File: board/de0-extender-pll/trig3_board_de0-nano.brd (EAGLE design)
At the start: 233.2 x 160 mm, 305 parts, among them IC1 ICL7660CPA, IC2 ICL7660CPA, IC3 ICL7660CPA, IC4 ICL7660CPA, J10 2p-2.54, J11 2p-2.54, J12 4p-2.54, J13 BU-SMB-V, J131 4p-2.54, J14 BU-SMB-V, J141 2p-2.54, J15 2p-2.54, J16 2p-2.54, J17 2p-2.54, J18 2p-2.54, J19 6HE-160-VG64AC, J20 4p-2.54, J21 4p-2.54, J22 2p-2.54, J23 2p-2.54, J24 2p-2.54, J25 2p-2.54, J26 4p-2.54, J27 4p-2.54, J28 2p-2.54, J29 2p-2.54, J3 4p-2.54, J30 2p-2.54, J31 2p-2.54, J311 4p-2.54, J32 2p-2.54, J33 2p-2.54, J34 2p-2.54, J35 2p-2.54, J36 2p-2.54, J37 2p-2.54, J38 2p-2.54, J39 2p-2.54, J4 2p-2.54, J40 2p-2.54, J41 2p-2.54, J42 2p-2.54, J43 2p-2.54, J48 2p-2.54, J49 2p-2.54, J5 2p-2.54, J50 2p-2.54, J51 2p-2.54, J52 2p-2.54, J53 2p-2.54, J54 2p-2.54, J55 2p-2.54, J6 2p-2.54, J7 4p-2.54, J8 2p-2.54, J9 2p-2.54, K15_R10P BU-SMB-V, K16_R10N BU-SMB-V, M16CLK_3N BU-SMB-V, P11 BU-SMB-V, P14_CLKOUT_4P BU-SMB-V, P15 BU-SMB-V, P16_R15N BU-SMB-V, P9 BU-SMB-V, T10_B16N BU-SMB-V, T12_B18N BU-SMB-V, T13_B20N BU-SMB-V, T14_B23P BU-SMB-V, T15_B23N BU-SMB-V, T9CLK_7N BU-SMB-V

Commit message: removed some unused inputs
kept all clock inputs and some extra inputs
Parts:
- removed A14_CLKOUT_2N, B7_T9P, C3_CLKOUT_3N, C9_T15N, D3_CLKOUT_3P, D9_T15P, G15_R5P, G16_R5N, N15_R13P, N16_R13N, P14_CLKOUT_4P, R10_B16P, R12_B18P, R14_CLKOUT_4N, T10_B16N, T12_B18N: BU-SMB-V, con-coax:BU-SMB-V
- removed J10, J11, J28, J29, J30, J31, J48, J49, J50, J51, J52, J53, J54, J55, J8, J9: 2p-2.54, Seeed-Connector:H2-2.54
- removed R100, R111, R141, R24, R26, R27, R29, R45, R46, R47, R49, R50, R51, R52, R53, R91: 50, SparkFun-Passives:AXIAL-0.3
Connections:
- net GND: no longer A14_CLKOUT_2N.2, A14_CLKOUT_2N.3, A14_CLKOUT_2N.4, A14_CLKOUT_2N.5, B7_T9P.2, B7_T9P.3, B7_T9P.4, B7_T9P.5, C3_CLKOUT_3N.2, C3_CLKOUT_3N.3, C3_CLKOUT_3N.4, C3_CLKOUT_3N.5, C9_T15N.2, C9_T15N.3, C9_T15N.4, C9_T15N.5, D3_CLKOUT_3P.2, D3_CLKOUT_3P.3, D3_CLKOUT_3P.4, D3_CLKOUT_3P.5, D9_T15P.2, D9_T15P.3, D9_T15P.4, D9_T15P.5, G15_R5P.2, G15_R5P.3, G15_R5P.4, G15_R5P.5, G16_R5N.2, G16_R5N.3, G16_R5N.4, G16_R5N.5, J10.1, J11.1, J28.1, J29.1, J30.1, J31.1, J48.1, J49.1, J50.1, J51.1, J52.1, J53.1, J54.1, J55.1, J8.1, J9.1, N15_R13P.2, N15_R13P.3, N15_R13P.4, N15_R13P.5, N16_R13N.2, N16_R13N.3, N16_R13N.4, N16_R13N.5, P14_CLKOUT_4P.2, P14_CLKOUT_4P.3, P14_CLKOUT_4P.4, P14_CLKOUT_4P.5, R100.P$1, R10_B16P.2, R10_B16P.3, R10_B16P.4, R10_B16P.5, R111.P$1, R12_B18P.2, R12_B18P.3, R12_B18P.4, R12_B18P.5, R141.P$1, R14_CLKOUT_4N.2, R14_CLKOUT_4N.3, R14_CLKOUT_4N.4, R14_CLKOUT_4N.5, R24.P$1, R26.P$1, R27.P$1, R29.P$1, R45.P$1, R46.P$1, R47.P$1, R49.P$1, R50.P$1, R51.P$1, R52.P$1, R53.P$1, R91.P$1, T10_B16N.2, T10_B16N.3, T10_B16N.4, T10_B16N.5, T12_B18N.2, T12_B18N.3, T12_B18N.4, T12_B18N.5
- net GPIO_00_D3: no longer D3_CLKOUT_3P.1, J50.2, R51.P$2
- net GPIO_012_B7: no longer B7_T9P.1, J49.2, R50.P$2
- net GPIO_01_C3: no longer C3_CLKOUT_3N.1, J30.2, R27.P$2
- net GPIO_024_C9: no longer C9_T15N.1, J8.2, R91.P$2
- net GPIO_025_D9: no longer D9_T15P.1, J11.2, R141.P$2
- net GPIO_111_R10: no longer J48.2, R10_B16P.1, R49.P$2
- net GPIO_122_R14: no longer J53.2, R14_CLKOUT_4N.1, R46.P$2
- net GPIO_123_N16: no longer J55.2, N16_R13N.1, R52.P$2
- net GPIO_124_N15: no longer J54.2, N15_R13P.1, R47.P$2
- net GPIO_125_P14: no longer J52.2, P14_CLKOUT_4P.1, R45.P$2
- net GPIO_15_T12: no longer J9.2, R100.P$2, T12_B18N.1
- net GPIO_16_R12: no longer J10.2, R111.P$2, R12_B18P.1
- net GPIO_18_T10: no longer J51.2, R53.P$2, T10_B16N.1
- net GPIO_20_A14: no longer A14_CLKOUT_2N.1, J31.2, R29.P$2
- net GPIO_211_G16: no longer G16_R5N.1, J28.2, R24.P$2
- net GPIO_212_G15: no longer G15_R5P.1, J29.2, R26.P$2
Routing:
- net GPIO_20_A14: track 151.6 -> 136.6 mm
- net GPIO_025_D9: track 140.6 -> 125.7 mm
- net GPIO_16_R12: track 100.3 -> 85.5 mm
- net GPIO_15_T12: track 91.4 -> 77.3 mm
- net GPIO_012_B7: track 137.2 -> 123.2 mm
- net GPIO_122_R14: track 105.3 -> 91.4 mm
- net GPIO_111_R10: track 133.7 -> 120.0 mm
- net GPIO_123_N16: track 105.6 -> 92.0 mm
- net GPIO_00_D3: track 125.2 -> 111.6 mm
- net GPIO_01_C3: track 120.4 -> 106.8 mm
- net GPIO_124_N15: track 144.3 -> 130.6 mm
- net GPIO_125_P14: track 101.0 -> 87.4 mm
- net GPIO_18_T10: track 109.7 -> 96.2 mm
- net GPIO_024_C9: track 120.8 -> 107.4 mm
- net GPIO_211_G16: track 59.4 -> 51.8 mm
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
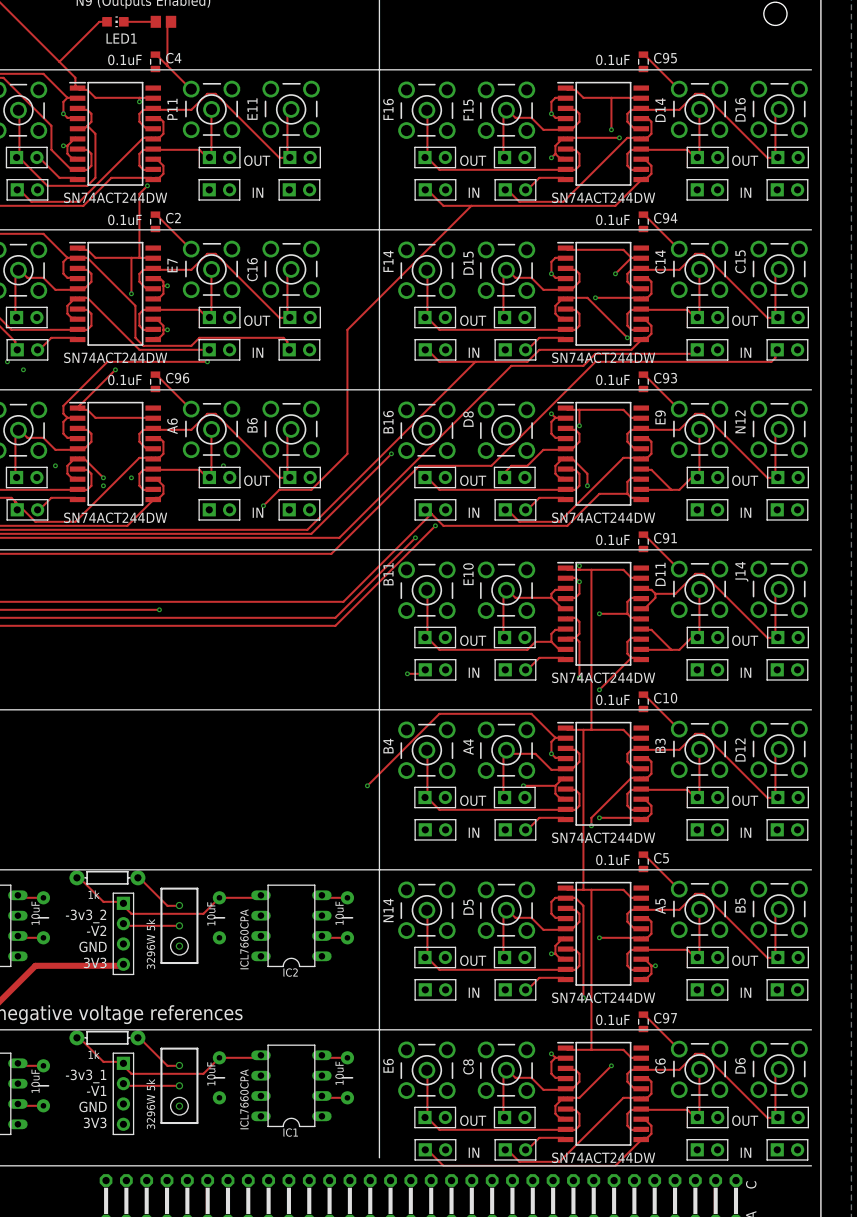
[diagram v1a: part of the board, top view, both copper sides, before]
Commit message: removed many outputs and negative voltage
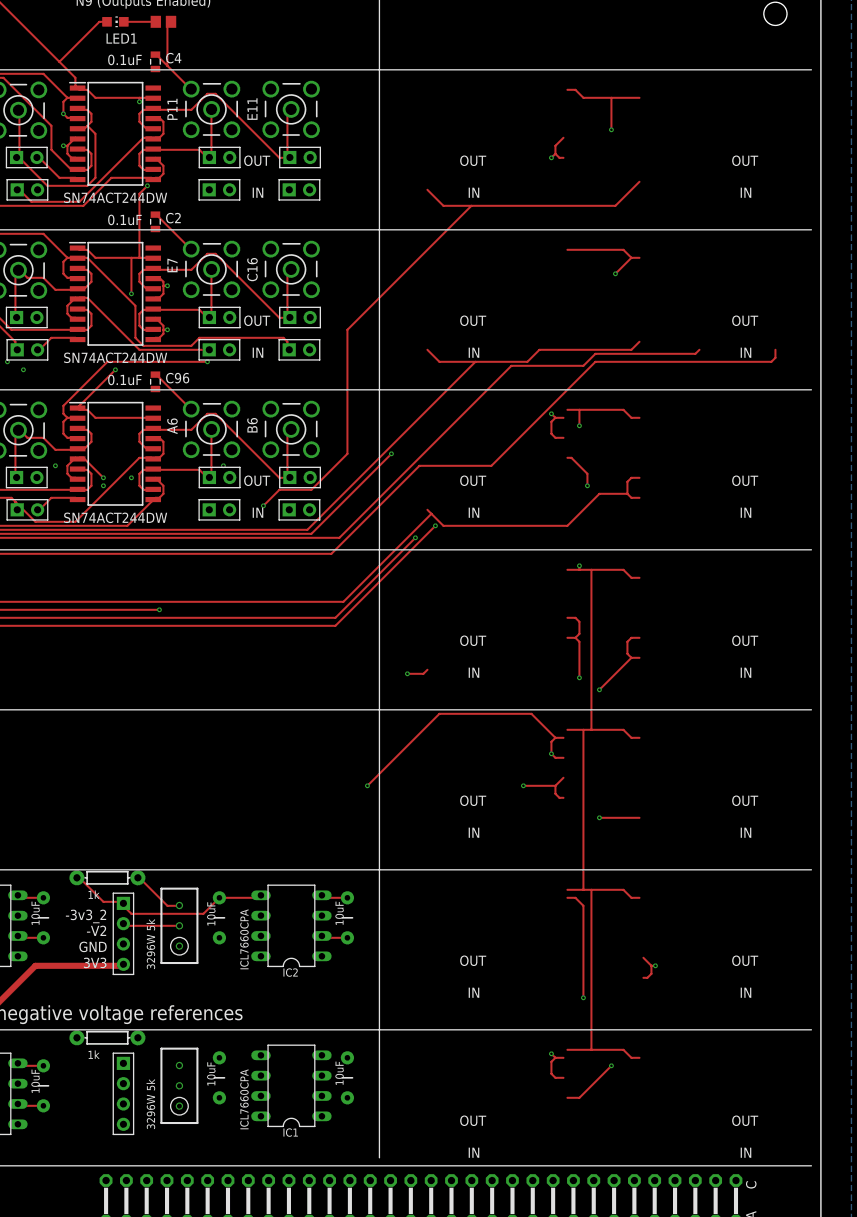
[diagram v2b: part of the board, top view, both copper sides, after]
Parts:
- removed A4, A5, B11, B16, B3, B4, B5, C14, C15, C6, C8, D11, D12, D14, D15, D16, D5, D6, D8, E10, E6, E9, F14, F15, F16, J14, N12, N14: BU-SMB-V, con-coax:BU-SMB-V
- removed C10, C5, C91, C93, C94, C95, C97: 0.1uF, SparkFun-Capacitors:0805
- removed OJ1, OJ17, OJ18, OJ19, OJ2, OJ20, OJ21, OJ22, OJ23, OJ24, OJ25, OJ26, OJ27, OJ28, OJ29, OJ3, OJ30, OJ31, OJ32, OJ33, OJ34, OJ35, OJ36, OJ37, OJ38, OJ39, OJ4, OJ40, OJ49, OJ5, OJ50, OJ51, OJ52, OJ53, OJ54, OJ55, OJ56, OJ6, OJ65, OJ66, OJ67, OJ68, OJ69, OJ7, OJ70, OJ71, OJ72, OJ8, OJ89, OJ90, OJ91, OJ92, OJ93, OJ94, OJ95, OJ96: 2p-2.54, Seeed-Connector:H2-2.54
- removed VSLUE, VSLUE11, VSLUE2, VSLUE3, VSLUE4, VSLUE6, VSLUE8: SN74ACT244DW, SN74ACT244DW:SOIC127P1030X265-20N
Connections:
- removed net OUT1: J14.1, OJ1.1, VSLUE.16, VSLUE.18
- removed net OUT10: E9.1, OJ19.1, VSLUE2.12, VSLUE2.14
- removed net OUT11: D8.1, OJ17.1, VSLUE2.3, VSLUE2.5
- removed net OUT12: B16.1, OJ18.1, VSLUE2.7, VSLUE2.9
- removed net OUT13: C15.1, OJ28.1, VSLUE3.16, VSLUE3.18
- removed net OUT14: C14.1, OJ27.1, VSLUE3.12, VSLUE3.14
- removed net OUT15: D15.1, OJ25.1, VSLUE3.3, VSLUE3.5
- removed net OUT16: F14.1, OJ26.1, VSLUE3.7, VSLUE3.9
- removed net OUT17: D16.1, OJ36.1, VSLUE4.16, VSLUE4.18
- removed net OUT18: D14.1, OJ35.1, VSLUE4.12, VSLUE4.14
- removed net OUT19: F15.1, OJ33.1, VSLUE4.3, VSLUE4.5
- removed net OUT2: D11.1, OJ2.1, VSLUE.12, VSLUE.14
- removed net OUT20: F16.1, OJ34.1, VSLUE4.7, VSLUE4.9
- removed net OUT25: D6.1, OJ52.1, VSLUE6.16, VSLUE6.18
- removed net OUT26: C6.1, OJ51.1, VSLUE6.12, VSLUE6.14
- removed net OUT27: C8.1, OJ49.1, VSLUE6.3, VSLUE6.5
- removed net OUT28: E6.1, OJ50.1, VSLUE6.7, VSLUE6.9
- removed net OUT3: B11.1, OJ3.1, VSLUE.7, VSLUE.9
- removed net OUT33: B5.1, OJ68.1, VSLUE8.16, VSLUE8.18
- removed net OUT34: A5.1, OJ67.1, VSLUE8.12, VSLUE8.14
- removed net OUT35: D5.1, OJ65.1, VSLUE8.3, VSLUE8.5
- removed net OUT36: N14.1, OJ66.1, VSLUE8.7, VSLUE8.9
- removed net OUT4: E10.1, OJ4.1, VSLUE.3, VSLUE.5
- removed net OUT45: D12.1, OJ92.1, VSLUE11.16, VSLUE11.18
- removed net OUT46: B3.1, OJ91.1, VSLUE11.12, VSLUE11.14
- removed net OUT47: A4.1, OJ89.1, VSLUE11.3, VSLUE11.5
- removed net OUT48: B4.1, OJ90.1, VSLUE11.7, VSLUE11.9
- removed net OUT9: N12.1, OJ20.1, VSLUE2.16, VSLUE2.18
- net 5V: no longer C10.2, C5.2, C91.2, C93.2, C94.2, C95.2, C97.2, VSLUE.20, VSLUE11.20, VSLUE2.20, VSLUE3.20, VSLUE4.20, VSLUE6.20, VSLUE8.20
- net GND: no longer A4.2, A4.3, A4.4, A4.5, A5.2, A5.3, A5.4, A5.5, B11.2, B11.3, B11.4, B11.5, B16.2, B16.3, B16.4, B16.5, B3.2, B3.3, B3.4, B3.5, B4.2, B4.3, B4.4, B4.5, B5.2, B5.3, B5.4, B5.5, C10.1, C14.2, C14.3, C14.4, C14.5, C15.2, C15.3, C15.4, C15.5, C5.1, C6.2, C6.3, C6.4, C6.5, C8.2, C8.3, C8.4, C8.5, C91.1, C93.1, C94.1, C95.1, C97.1, D11.2, D11.3, D11.4, D11.5, D12.2, D12.3, D12.4, D12.5, D14.2, D14.3, D14.4, D14.5, D15.2, D15.3, D15.4, D15.5, D16.2, D16.3, D16.4, D16.5, D5.2, D5.3, D5.4, D5.5, D6.2, D6.3, D6.4, D6.5, D8.2, D8.3, D8.4, D8.5, E10.2, E10.3, E10.4, E10.5, E6.2, E6.3, E6.4, E6.5, E9.2, E9.3, E9.4, E9.5, F14.2, F14.3, F14.4, F14.5, F15.2, F15.3, F15.4, F15.5, F16.2, F16.3, F16.4, F16.5, J14.2, J14.3, J14.4, J14.5, N12.2, N12.3, N12.4, N12.5, N14.2, N14.3, N14.4, N14.5, OJ1.2, OJ17.2, OJ18.2, OJ19.2, OJ2.2, OJ20.2, OJ21.2, OJ22.2, OJ23.2, OJ24.2, OJ25.2, OJ26.2, OJ27.2, OJ28.2, OJ29.2, OJ3.2, OJ30.2, OJ31.2, OJ32.2, OJ33.2, OJ34.2, OJ35.2, OJ36.2, OJ37.2, OJ38.2, OJ39.2, OJ4.2, OJ40.2, OJ49.2, OJ5.2, OJ50.2, OJ51.2, OJ52.2, OJ53.2, OJ54.2, OJ55.2, OJ56.2, OJ6.2, OJ65.2, OJ66.2, OJ67.2, OJ68.2, OJ69.2, OJ7.2, OJ70.2, OJ71.2, OJ72.2, OJ8.2, OJ89.2, OJ90.2, OJ91.2, OJ92.2, OJ93.2, OJ94.2, OJ95.2, OJ96.2, VSLUE.10, VSLUE11.10, VSLUE2.10, VSLUE3.10, VSLUE4.10, VSLUE6.10, VSLUE8.10
- net GPIO_013_D6: no longer OJ55.1, VSLUE6.2, VSLUE6.4
- net GPIO_015_C6: no longer OJ56.1, VSLUE6.6, VSLUE6.8
- net GPIO_016_C8: no longer OJ53.1, VSLUE6.15, VSLUE6.17
- net GPIO_017_E6: no longer OJ54.1, VSLUE6.11, VSLUE6.13
- net GPIO_019_D8: no longer OJ21.1, VSLUE2.15, VSLUE2.17
- net GPIO_023_E9: no longer OJ24.1, VSLUE2.6, VSLUE2.8
- net GPIO_027_E10: no longer OJ5.1, VSLUE.15, VSLUE.17
- net GPIO_029_B11: no longer OJ6.1, VSLUE.11, VSLUE.13
- net GPIO_031_D11: no longer OJ8.1, VSLUE.6, VSLUE.8
- net GPIO_032_D12: no longer OJ95.1, VSLUE11.2, VSLUE11.4
- net GPIO_04_B3: no longer OJ96.1, VSLUE11.6, VSLUE11.8
- net GPIO_05_B4: no longer OJ94.1, VSLUE11.11, VSLUE11.13
- net GPIO_06_A4: no longer OJ93.1, VSLUE11.15, VSLUE11.17
- net GPIO_07_B5: no longer OJ71.1, VSLUE8.2, VSLUE8.4
- net GPIO_08_A5: no longer OJ72.1, VSLUE8.6, VSLUE8.8
- net GPIO_09_D5: no longer OJ69.1, VSLUE8.15, VSLUE8.17
- net GPIO_112_N12: no longer OJ23.1, VSLUE2.2, VSLUE2.4
- net GPIO_114_N9: no longer VSLUE.1, VSLUE.19, VSLUE11.1, VSLUE11.19, VSLUE2.1, VSLUE2.19, VSLUE3.1, VSLUE3.19, VSLUE4.1, VSLUE4.19, VSLUE6.1, VSLUE6.19, VSLUE8.1, VSLUE8.19
- net GPIO_127_N14: no longer OJ70.1, VSLUE8.11, VSLUE8.13
- net GPIO_133_J14: no longer OJ7.1, VSLUE.2, VSLUE.4
- net GPIO_210_F14: no longer OJ30.1, VSLUE3.11, VSLUE3.13
- net GPIO_21_B16: no longer OJ22.1, VSLUE2.11, VSLUE2.13
- net GPIO_22_C14: no longer OJ32.1, VSLUE3.6, VSLUE3.8
- net GPIO_24_C15: no longer OJ31.1, VSLUE3.2, VSLUE3.4
- net GPIO_25_D16: no longer OJ39.1, VSLUE4.2, VSLUE4.4
- net GPIO_26_D15: no longer OJ29.1, VSLUE3.15, VSLUE3.17
- net GPIO_27_D14: no longer OJ40.1, VSLUE4.6, VSLUE4.8
- net GPIO_28_F15: no longer OJ37.1, VSLUE4.15, VSLUE4.17
- net GPIO_29_F16: no longer OJ38.1, VSLUE4.11, VSLUE4.13
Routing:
- net GPIO_017_E6: track 182.5 -> 45.2 mm
- net GND: track 141.6 -> 57.0 mm
- net GPIO_25_D16: track 368.8 -> 330.0 mm, vias 1 -> 0
- net GPIO_24_C15: track 193.8 -> 155.1 mm, vias 2 -> 1
- net 3V3: track 318.8 -> 281.0 mm
- net GPIO_133_J14: track 265.4 -> 230.4 mm, vias 2 -> 1
- net OUT25: track 33.0 -> 0.00 mm
- net OUT45: track 33.0 -> 0.00 mm
- net OUT33: track 33.0 -> 0.00 mm
- net OUT9: track 33.0 -> 0.00 mm
- net OUT17: track 33.0 -> 0.00 mm
- net OUT13: track 33.0 -> 0.00 mm
- net OUT1: track 31.1 -> 0.00 mm
- net OUT12: track 29.6 -> 0.00 mm
- net OUT48: track 29.6 -> 0.00 mm
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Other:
- board text removed: "-3v3_1"

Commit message: more removal
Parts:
- removed C1, C12, C13, C17, C18, C3, C7, C9: 10uF, SparkFun-Capacitors:CAP-PTH-5MM
- removed C19, C20, C21, C22: 0.1uF, SparkFun-Capacitors:0805
- removed IC1, IC2, IC3, IC4: ICL7660CPA, maxim:DIL08
- removed J1: (no value), SparkFun-Connectors:2X13
- removed J131, J20, J21, J26, J27, J311: 4p-2.54, Seeed-Connector:H4-2.54
- removed J19: 6HE-160-VG64AC, 19inch:6HE_160-VG64AC
- removed OJ10, OJ11, OJ12, OJ9: 2p-2.54, Seeed-Connector:H2-2.54
- removed R1, R2, R3, R7: 3296W 5k, resistor:RTRIM3296W
- removed R10, R12, R13, R14: 1k, SparkFun-Passives:AXIAL-0.3
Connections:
- removed net -3V3_1: C3.1, IC1.5, J20.1, R10.P$2
- removed net -3V3_2: C9.1, IC2.5, J21.1, R12.P$2
- removed net -3V3_3: C13.1, IC3.5, J26.1, R13.P$2
- removed net -3V3_4: C18.1, IC4.5, J27.1, R14.P$2
- removed net -V1: C19.2, J20.2, OJ9.1, R1.2
- removed net -V2: C20.2, J21.2, OJ10.1, R2.2
- removed net -V3: C21.2, J26.2, OJ11.1, R3.2
- removed net -V4: C22.2, J27.2, OJ12.1, R7.2
- removed net AIN0: J1.24, J131.4
- removed net AIN1: J1.25, J311.1
- removed net AIN2: J1.22, J131.3
- removed net AIN3: J1.21, J311.3
- removed net AIN4: J1.23, J311.2
- removed net AIN5: J1.18, J131.1
- removed net AIN6: J1.19, J311.4
- removed net AIN7: J1.20, J131.2
- removed net GPIO_20_A14: J1.5
- removed net GPIO_210_F14: J1.15
- removed net GPIO_211_G16: J1.16
- removed net GPIO_212_G15: J1.17
- removed net GPIO_21_B16: J1.6
- removed net GPIO_22_C14: J1.7
- removed net GPIO_24_C15: J1.9
- removed net GPIO_25_D16: J1.10
- removed net GPIO_26_D15: J1.11
- removed net GPIO_27_D14: J1.12
- removed net GPIO_28_F15: J1.13
- removed net GPIO_29_F16: J1.14
- removed net N$1: C1.1, IC1.2
- removed net N$10: R1.3, R10.P$1
- removed net N$11: R12.P$1, R2.3
- removed net N$12: R13.P$1, R3.3
- removed net N$13: R14.P$1, R7.3
- removed net N$2: C1.2, IC1.4
- removed net N$3: C12.1, IC3.2
- removed net N$4: C7.1, IC2.2
- removed net N$5: C7.2, IC2.4
- removed net N$6: C12.2, IC3.4
- removed net N$7: C17.1, IC4.2
- removed net N$8: C17.2, IC4.4
- net 3V3: no longer IC1.8, IC2.8, IC3.8, IC4.8, J1.1, J20.4, J21.4, J26.4, J27.4
- net 5V: no longer J19.1-A32, J19.1-C32, J19.2-A32, J19.2-C32
- net GND: no longer C13.2, C18.2, C19.1, C20.1, C21.1, C22.1, C3.2, C9.2, IC1.3, IC2.3, IC3.3, IC4.3, J1.26, J19.1-A9, J19.1-C9, J19.2-A9, J19.2-C9, J20.3, J21.3, J26.3, J27.3, R1.1, R2.1, R3.1, R7.1
- net GPIO_014_A7: no longer OJ9.2
- net GPIO_020_E8: no longer OJ12.2
- net GPIO_030_A12: no longer OJ10.2
- net GPIO_11_T15: no longer OJ11.2
- net GPIO_23_C16: no longer J1.8
- net GPIO_2_IN0_E15CLK: no longer J1.2
- net GPIO_2_IN1_E16CLK: no longer J1.3
- net GPIO_2_IN2_M16CLK: no longer J1.4
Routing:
- net GPIO_114_N9: track 431.7 -> 0.00 mm, vias 9 -> 0
- net GPIO_25_D16: track 330.0 -> 0.00 mm
- net 3V3: track 281.0 -> 0.00 mm
- net GPIO_127_N14: track 251.8 -> 0.00 mm, vias 2 -> 0
- net GPIO_133_J14: track 230.4 -> 0.00 mm, vias 1 -> 0
- net GPIO_08_A5: track 211.4 -> 0.00 mm
- net GPIO_112_N12: track 206.3 -> 0.00 mm, vias 2 -> 0
- net GPIO_07_B5: track 199.1 -> 0.00 mm, vias 2 -> 0
- net GPIO_013_D6: track 193.1 -> 0.00 mm, vias 2 -> 0
- net GPIO_015_C6: track 182.2 -> 0.00 mm, vias 1 -> 0
- net GPIO_27_D14: track 174.4 -> 0.00 mm, vias 3 -> 0
- net GPIO_28_F15: track 173.2 -> 0.00 mm, vias 1 -> 0
- net GPIO_29_F16: track 169.9 -> 0.00 mm, vias 2 -> 0
- net GPIO_04_B3: track 160.2 -> 0.00 mm, vias 1 -> 0
- net GPIO_032_D12: track 159.9 -> 0.00 mm, vias 3 -> 0
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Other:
- board size 233.2 x 160 mm -> 50.5 x 62 mm
